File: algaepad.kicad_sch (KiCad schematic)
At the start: 65 parts, among them SW1 SW_Push, SW10 SW_Push, SW11 SW_Push, SW12 SW_Push, SW13 SW_Push, SW14 SW_Push, SW15 SW_Push, SW16 SW_Push, SW17 SW_Push, SW18 SW_Push, SW19 SW_Push, SW2 SW_Push, SW20 SW_Push, SW21 SW_Push, SW22 SW_Push, SW23 SW_Push, SW24 SW_Push, SW25 SW_Push, SW26 SW_Push, SW27 SW_Push, SW28 SW_Push, SW29 SW_Push, SW3 SW_Push, SW30 SW_Push, SW31 SW_Push, SW32 SW_Push, SW4 SW_Push, SW5 SW_Push, SW6 SW_Push, SW7 SW_Push, SW8 SW_Push, SW9 SW_Push, U1 Elite-C

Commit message: fix up footprints so basic layout can be started
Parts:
- D1, D10, D11, D12, D13, D14, D15, D16, D17, D18, D19, D2, D20, D21, D22, D23, D24, D25, D26, D27, D28, D29, D3, D30, D31, D32, D4, D5, D6, D7, D8, D9: footprint reversible-kicad-footprints:D_SOD-123 -> reversible-footprints:D_SOD-123
- SW1, SW10, SW11, SW12, SW13, SW14, SW15, SW16, SW17, SW18, SW19, SW2, SW20, SW21, SW22, SW23, SW24, SW25, SW26, SW27, SW28, SW29, SW3, SW30, SW31, SW32, SW4, SW5, SW6, SW7, SW8, SW9: footprint reversible-kicad-footprints:MX-1U-Hotswap-NoBorder -> reversible-footprints:MX-1U-Hotswap

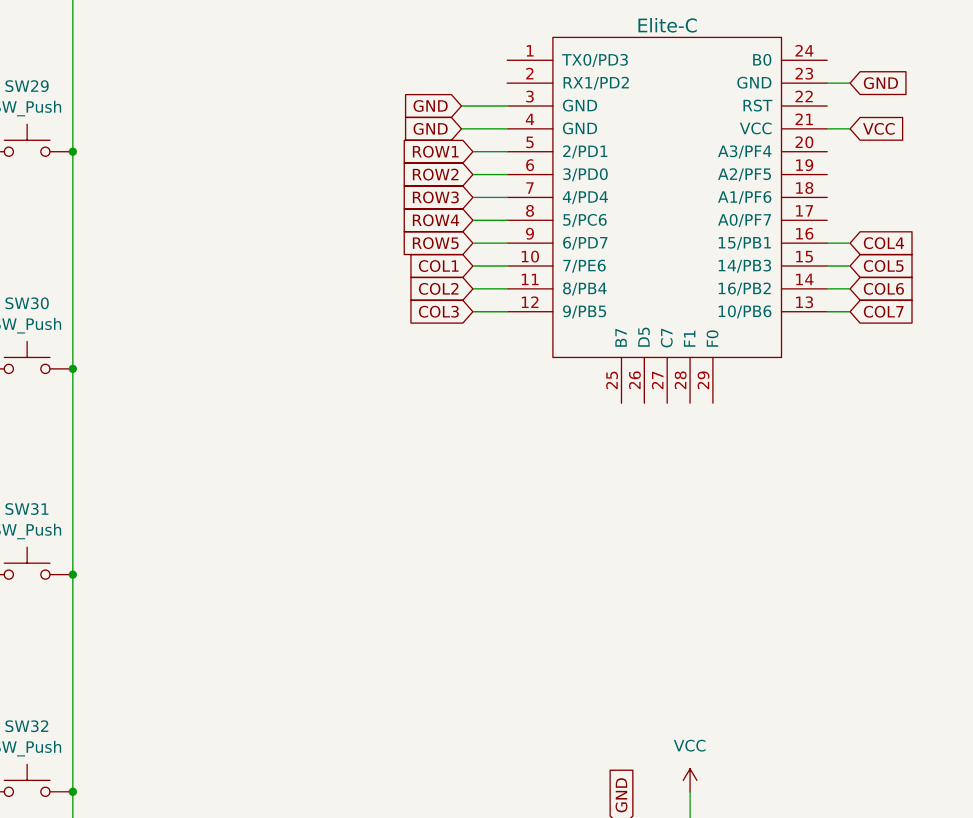
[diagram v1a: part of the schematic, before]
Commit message: add adafruit joystick symbol in a custom algaepad library
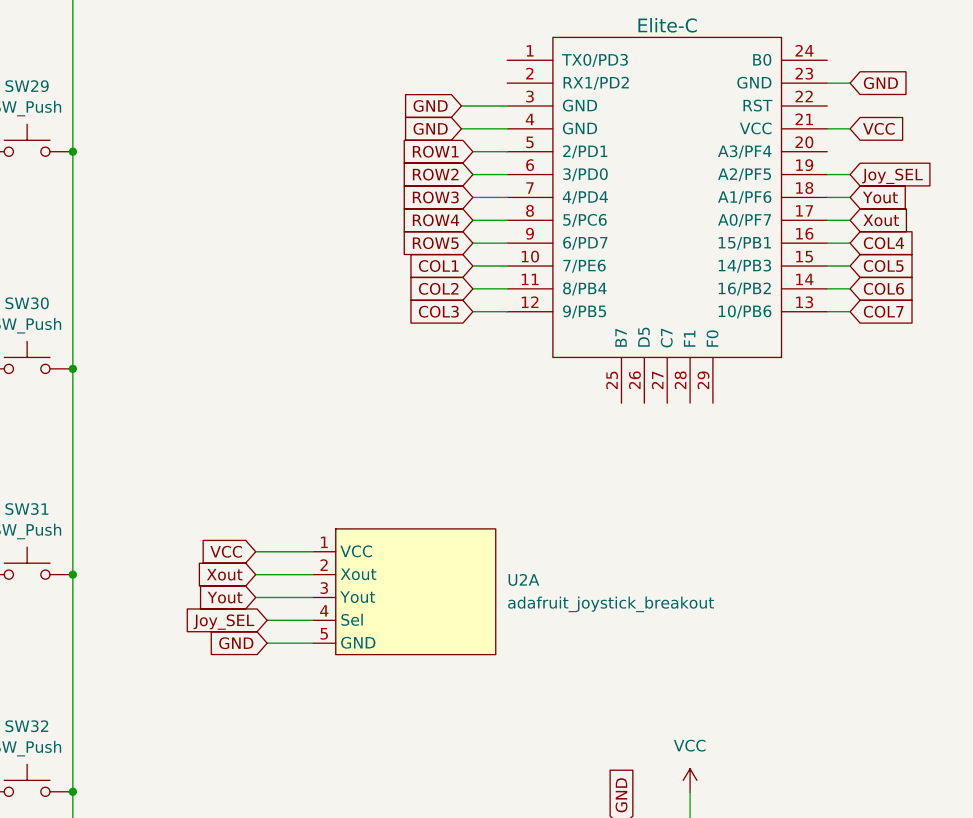
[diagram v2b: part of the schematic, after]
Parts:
- added U2: adafruit_joystick_breakout, symbol algaepad-library:adafruit_joystick_breakout
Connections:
- net GND: now also U2.5 (GND)
- net VCC: now also U2.1 (VCC)
- net Xout: now reaches U1.17 (A0/PF7)
- net Xout: now also U2.2 (Xout)
- net Yout: now reaches U1.18 (A1/PF6)
- net Yout: now also U2.3 (Yout)
- net Joy_SEL: now reaches U1.19 (A2/PF5)
- net Joy_SEL: now also U2.4 (Sel)
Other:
- title: Algaepad V1.0 -> AlgaePad
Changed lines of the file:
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@@
   (paper "A4")
   (title_block
-    (title "Algaepad V1.0")
+    (title "AlgaePad")
+    (rev "1.0")
     (company "by Seth Barbreree")
   )
@@
     (stroke (width 0) (type default) (color 0 0 0 0))
   )
+  (wire (pts (xy 257.81 59.69) (xy 260.35 59.69))
+    (stroke (width 0) (type default) (color 0 0 0 0))
+  )
   (wire (pts (xy 102.87 109.22) (xy 123.19 109.22))
     (stroke (width 0) (type default) (color 0 0 0 0))
@@
     (stroke (width 0) (type default) (color 0 0 0 0))
   )
+  (wire (pts (xy 194.31 104.14) (xy 200.66 104.14))
+    (stroke (width 0) (type default) (color 0 0 0 0))
+  )
   (wire (pts (xy 133.35 125.73) (xy 133.35 139.7))
     (stroke (width 0) (type default) (color 0 0 0 0))
@@
     (stroke (width 0) (type default) (color 0 0 0 0))
   )
+  (wire (pts (xy 257.81 57.15) (xy 260.35 57.15))
+    (stroke (width 0) (type default) (color 0 0 0 0))
+  )
   (wire (pts (xy 257.81 52.07) (xy 260.35 52.07))
     (stroke (width 0) (type default) (color 0 0 0 0))
@@
     (stroke (width 0) (type default) (color 0 0 0 0))
   )
+  (wire (pts (xy 194.31 99.06) (xy 200.66 99.06))
+    (stroke (width 0) (type default) (color 0 0 0 0))
+  )
   (wire (pts (xy 82.55 86.36) (xy 102.87 86.36))
     (stroke (width 0) (type default) (color 0 0 0 0))
@@
     (stroke (width 0) (type default) (color 0 0 0 0))
   )
+  (wire (pts (xy 257.81 62.23) (xy 260.35 62.23))
+    (stroke (width 0) (type default) (color 0 0 0 0))
+  )
   (wire (pts (xy 52.07 101.6) (xy 52.07 139.7))
     (stroke (width 0) (type default) (color 0 0 0 0))
@@
     (stroke (width 0) (type default) (color 0 0 0 0))
   )
+  (wire (pts (xy 195.58 109.22) (xy 200.66 109.22))
+    (stroke (width 0) (type default) (color 0 0 0 0))
+  )
   (wire (pts (xy 123.19 109.22) (xy 143.51 109.22))
     (stroke (width 0) (type default) (color 0 0 0 0))
@@
     (stroke (width 0) (type default) (color 0 0 0 0))
   )
+  (wire (pts (xy 195.58 106.68) (xy 200.66 106.68))
+    (stroke (width 0) (type default) (color 0 0 0 0))
+  )
   (wire (pts (xy 173.99 78.74) (xy 173.99 101.6))
     (stroke (width 0) (type default) (color 0 0 0 0))
@@
   )
   (wire (pts (xy 34.29 62.23) (xy 41.91 62.23))
+    (stroke (width 0) (type default) (color 0 0 0 0))
+  )
+  (wire (pts (xy 194.31 101.6) (xy 200.66 101.6))
     (stroke (width 0) (type default) (color 0 0 0 0))
   )
@@
     (effects (font (size 1.27 1.27)) (justify right))
     (property "Intersheet References" "${INTERSHEET_REFS}" (id 0) (at 210.7655 62.1506 0)
+      (effects (font (size 1.27 1.27)) (justify right) hide)
+    )
+  )
+  (global_label "GND" (shape input) (at 195.58 109.22 180) (fields_autoplaced)
+    (effects (font (size 1.27 1.27)) (justify right))
+    (property "Intersheet References" "${INTERSHEET_REFS}" (id 0) (at 189.2964 109.2994 0)
       (effects (font (size 1.27 1.27)) (justify right) hide)
     )
@@
     )
   )
+  (global_label "Yout" (shape input) (at 194.31 104.14 180) (fields_autoplaced)
+    (effects (font (size 1.27 1.27)) (justify right))
+    (property "Intersheet References" "${INTERSHEET_REFS}" (id 0) (at 187.7845 104.2194 0)
+      (effects (font (size 1.27 1.27)) (justify right) hide)
+    )
+  )
+  (global_label "Xout" (shape input) (at 260.35 62.23 0) (fields_autoplaced)
+    (effects (font (size 1.27 1.27)) (justify left))
+    (property "Intersheet References" "${INTERSHEET_REFS}" (id 0) (at 266.9964 62.1506 0)
+      (effects (font (size 1.27 1.27)) (justify left) hide)
+    )
+  )
+  (global_label "Joy_SEL" (shape input) (at 195.58 106.68 180) (fields_autoplaced)
+    (effects (font (size 1.27 1.27)) (justify right))
+    (property "Intersheet References" "${INTERSHEET_REFS}" (id 0) (at 185.7283 106.7594 0)
+      (effects (font (size 1.27 1.27)) (justify right) hide)
+    )
+  )
   (global_label "COL5" (shape input) (at 260.35 67.31 0) (fields_autoplaced)
     (effects (font (size 1.27 1.27)) (justify left))
@@
     )
   )
+  (global_label "Joy_SEL" (shape input) (at 260.35 57.15 0) (fields_autoplaced)
+    (effects (font (size 1.27 1.27)) (justify left))
+    (property "Intersheet References" "${INTERSHEET_REFS}" (id 0) (at 270.2017 57.0706 0)
+      (effects (font (size 1.27 1.27)) (justify left) hide)
+    )
+  )
   (global_label "COL2" (shape output) (at 72.39 139.7 270) (fields_autoplaced)
     (effects (font (size 1.27 1.27)) (justify right))
@@
     (effects (font (size 1.27 1.27)) (justify right))
     (property "Intersheet References" "${INTERSHEET_REFS}" (id 0) (at 210.8864 52.1494 0)
+      (effects (font (size 1.27 1.27)) (justify right) hide)
+    )
+  )
+  (global_label "Xout" (shape input) (at 194.31 101.6 180) (fields_autoplaced)
+    (effects (font (size 1.27 1.27)) (justify right))
+    (property "Intersheet References" "${INTERSHEET_REFS}" (id 0) (at 187.6636 101.6794 0)
       (effects (font (size 1.27 1.27)) (justify right) hide)
     )
@@
     )
   )
+  (global_label "Yout" (shape input) (at 260.35 59.69 0) (fields_autoplaced)
+    (effects (font (size 1.27 1.27)) (justify left))
+    (property "Intersheet References" "${INTERSHEET_REFS}" (id 0) (at 266.8755 59.6106 0)
+      (effects (font (size 1.27 1.27)) (justify left) hide)
+    )
+  )
   (global_label "COL1" (shape input) (at 218.44 67.31 180) (fields_autoplaced)
     (effects (font (size 1.27 1.27)) (justify right))
@@
     )
   )
+  (global_label "VCC" (shape input) (at 194.31 99.06 180) (fields_autoplaced)
+    (effects (font (size 1.27 1.27)) (justify right))
+    (property "Intersheet References" "${INTERSHEET_REFS}" (id 0) (at 188.2683 98.9806 0)
+      (effects (font (size 1.27 1.27)) (justify right) hide)
+    )
+  )
   (global_label "ROW2" (shape input) (at 218.44 57.15 180) (fields_autoplaced)
     (effects (font (size 1.27 1.27)) (justify right))
@@
     (pin "1")
     (pin "2")
+  )
+  (symbol (lib_id "algaepad-library:adafruit_joystick_breakout") (at 212.09 93.98 0) (unit 1)
+    (in_bom yes) (on_board no) (fields_autoplaced)
+    (property "Reference" "U2" (id 0) (at 222.25 102.2349 0)
+      (effects (font (size 1.27 1.27)) (justify left))
+    )
+    (property "Value" "adafruit_joystick_breakout" (id 1) (at 222.25 104.7749 0)
+      (effects (font (size 1.27 1.27)) (justify left))
+    )
+    (property "Footprint" "" (id 2) (at 212.09 93.98 0)
+      (effects (font (size 1.27 1.27)) hide)
+    )
+    (property "Datasheet" "" (id 3) (at 212.09 93.98 0)
+      (effects (font (size 1.27 1.27)) hide)
+    )
+    (pin "1")
+    (pin "2")
+    (pin "3")
+    (pin "4")
+    (pin "5")
+    (pin "1-UB")
+    (pin "2-UB")
+    (pin "1-UC")
+    (pin "2-UC")
+    (pin "1-UD")
+    (pin "2-UD")
+    (pin "1-UE")
+    (pin "2-UE")
   )
   (symbol (lib_id "Switch:SW_Push") (at 128.27 101.6 0) (unit 1)
@@
       (reference "U1") (unit 1) (value "Elite-C") (footprint "")
     )
-  )
+    (path "/35a9cb46-fe1e-43f3-af6e-d1f47b4e13be"
+      (reference "U2") (unit 1) (value "adafruit_joystick_breakout") (footprint "")
+    )
+  )

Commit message: first attempt at complete pcb layout
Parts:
- U1: footprint (none) -> keebio-parts:Elite-C
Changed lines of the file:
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@@
       (effects (font (size 1.524 1.524)))
     )
-    (property "Footprint" "" (at 266.7 121.92 90)
+    (property "Footprint" "keebio-parts:Elite-C" (at 266.7 121.92 90)
       (effects (font (size 1.524 1.524)) hide)
     )

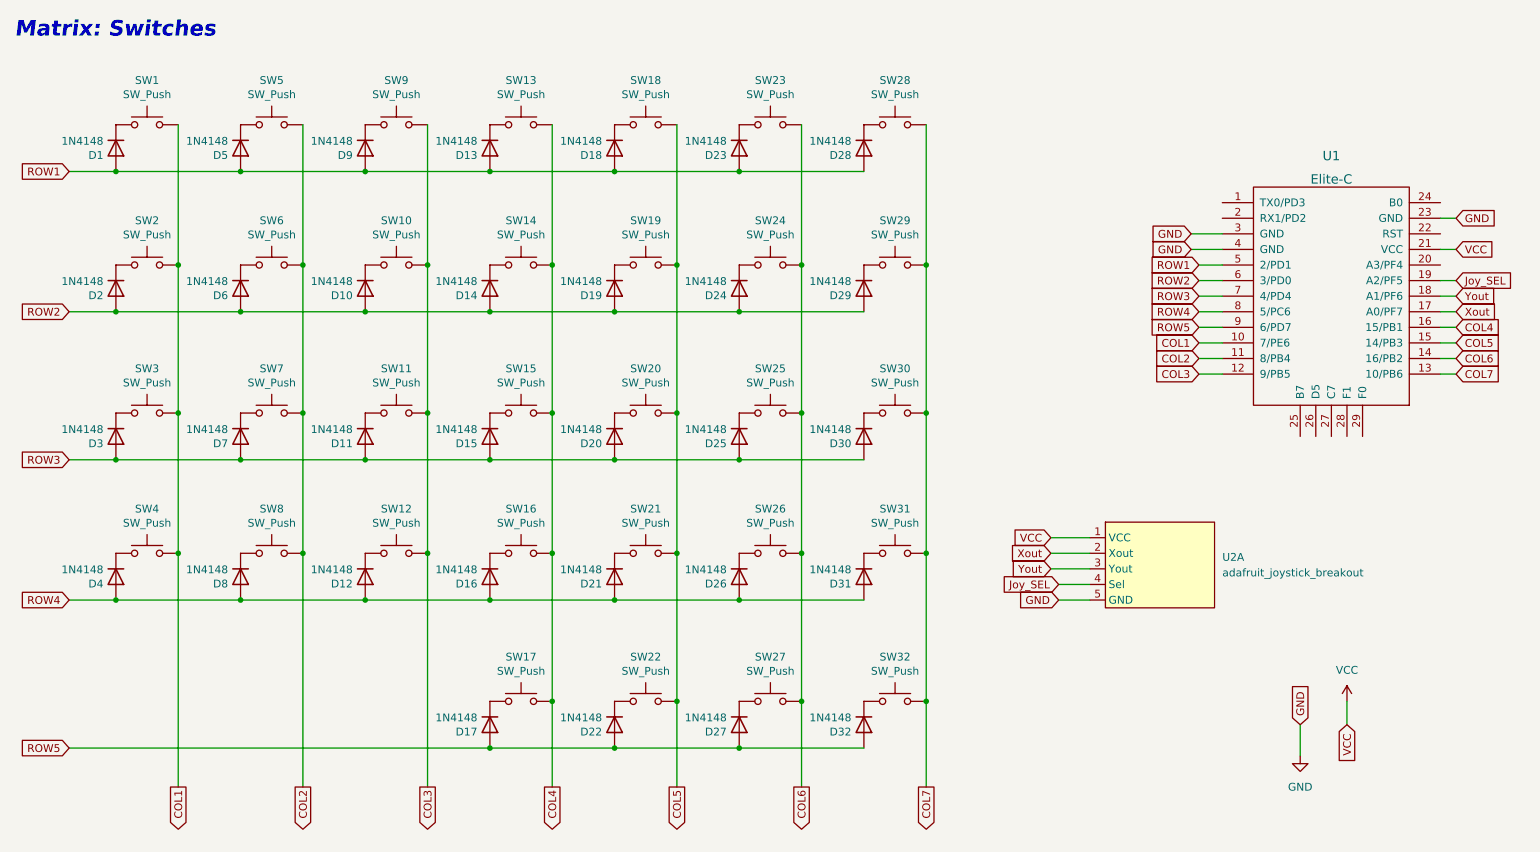
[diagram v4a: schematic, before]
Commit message: switch to SMT diode
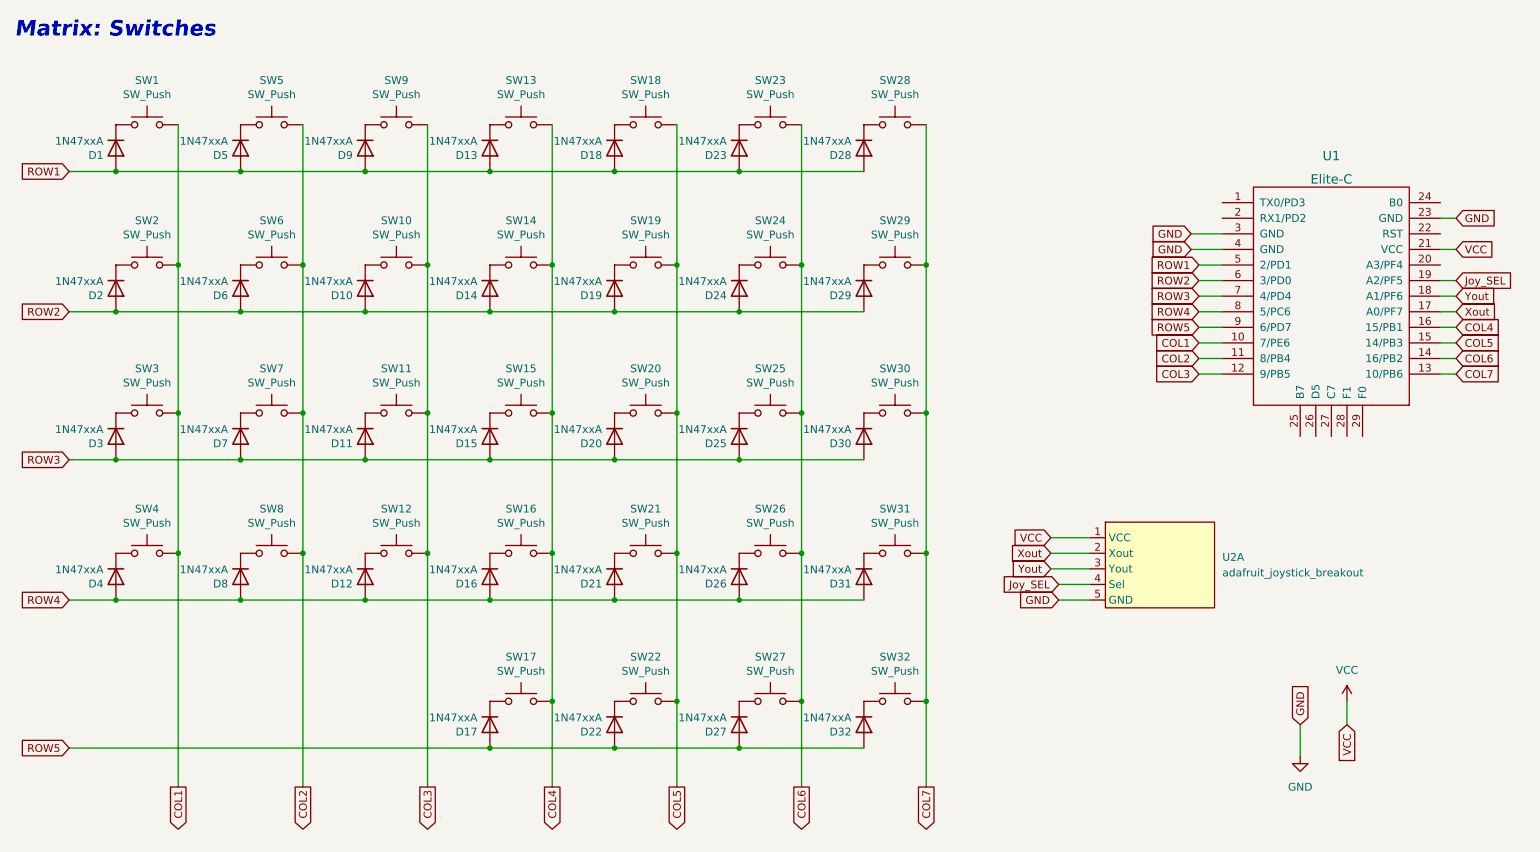
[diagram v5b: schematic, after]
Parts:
- D1, D10, D11, D12, D13, D14, D15, D16, D17, D18, D19, D2, D20, D21, D22, D23, D24, D25, D26, D27, D28, D29, D3, D30, D31, D32, D4, D5, D6, D7, D8, D9: value 1N4148 -> 1N47xxA; footprint reversible-footprints:D_SOD-123 -> Diode_THT:D_DO-41_SOD81_P10.16mm_Horizontal
